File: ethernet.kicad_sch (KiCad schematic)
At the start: 28 parts, among them J1 HR911105A, U4 LAN8742A, Y1 Crystal_GND24

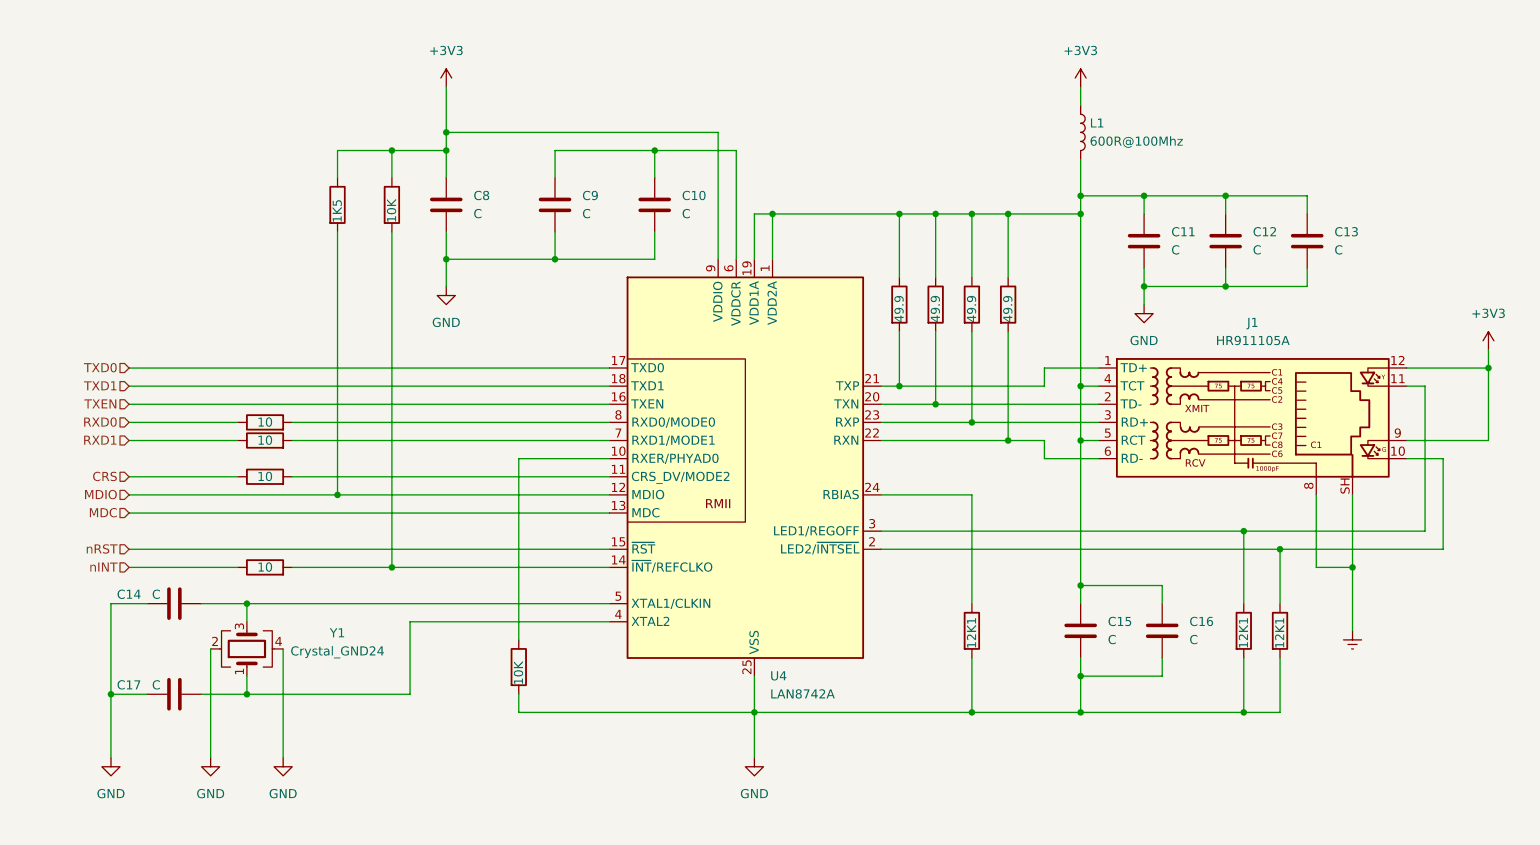
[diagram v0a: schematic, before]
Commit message: Rearranged sheets and corrected some namings
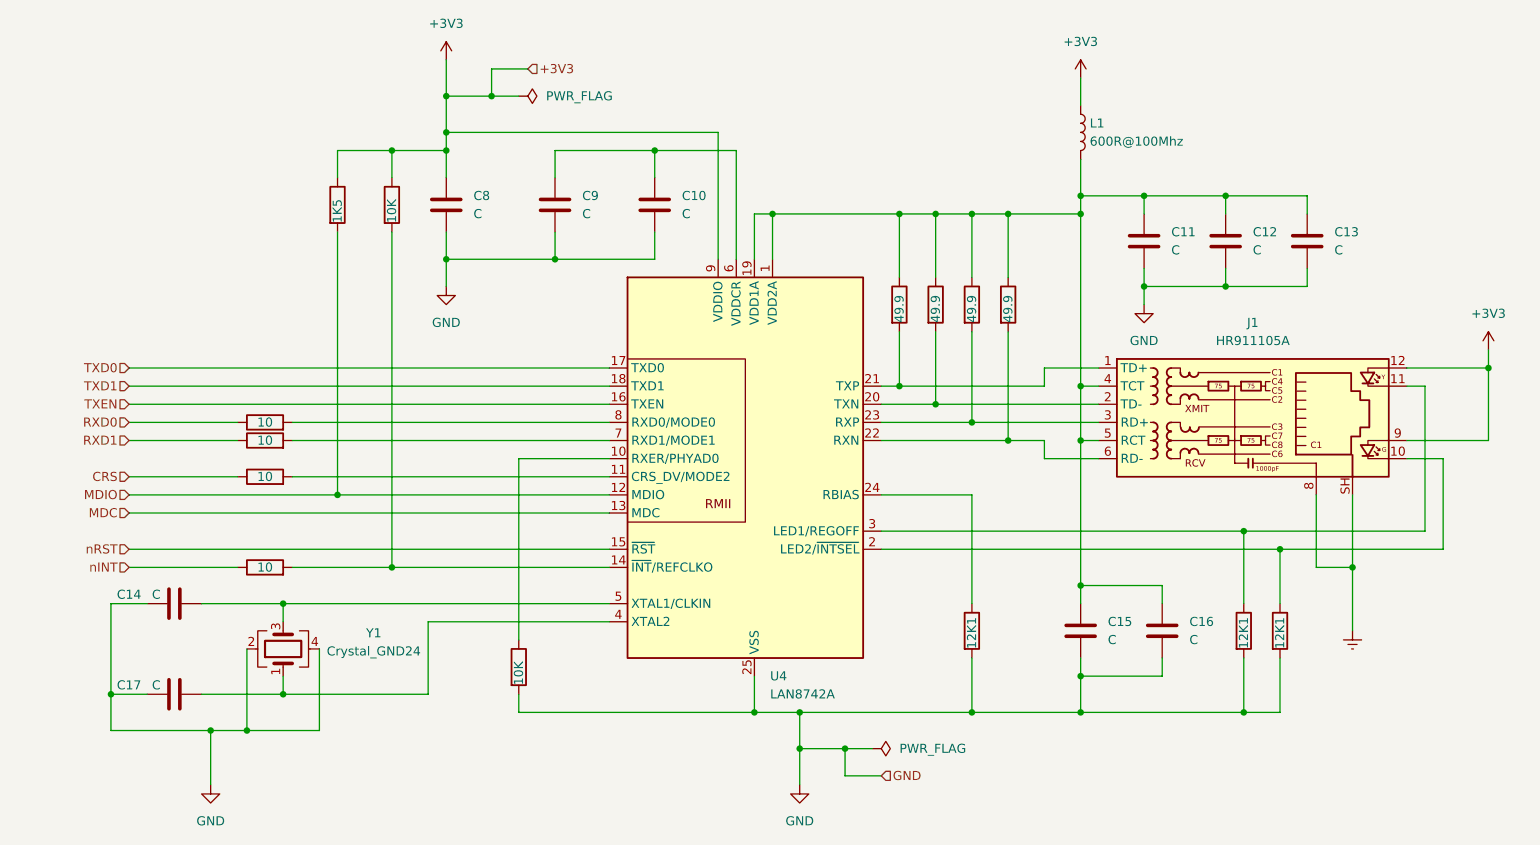
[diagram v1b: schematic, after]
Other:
- moved on the sheet: Y1

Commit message: Finished power setup and cleared some mistakes
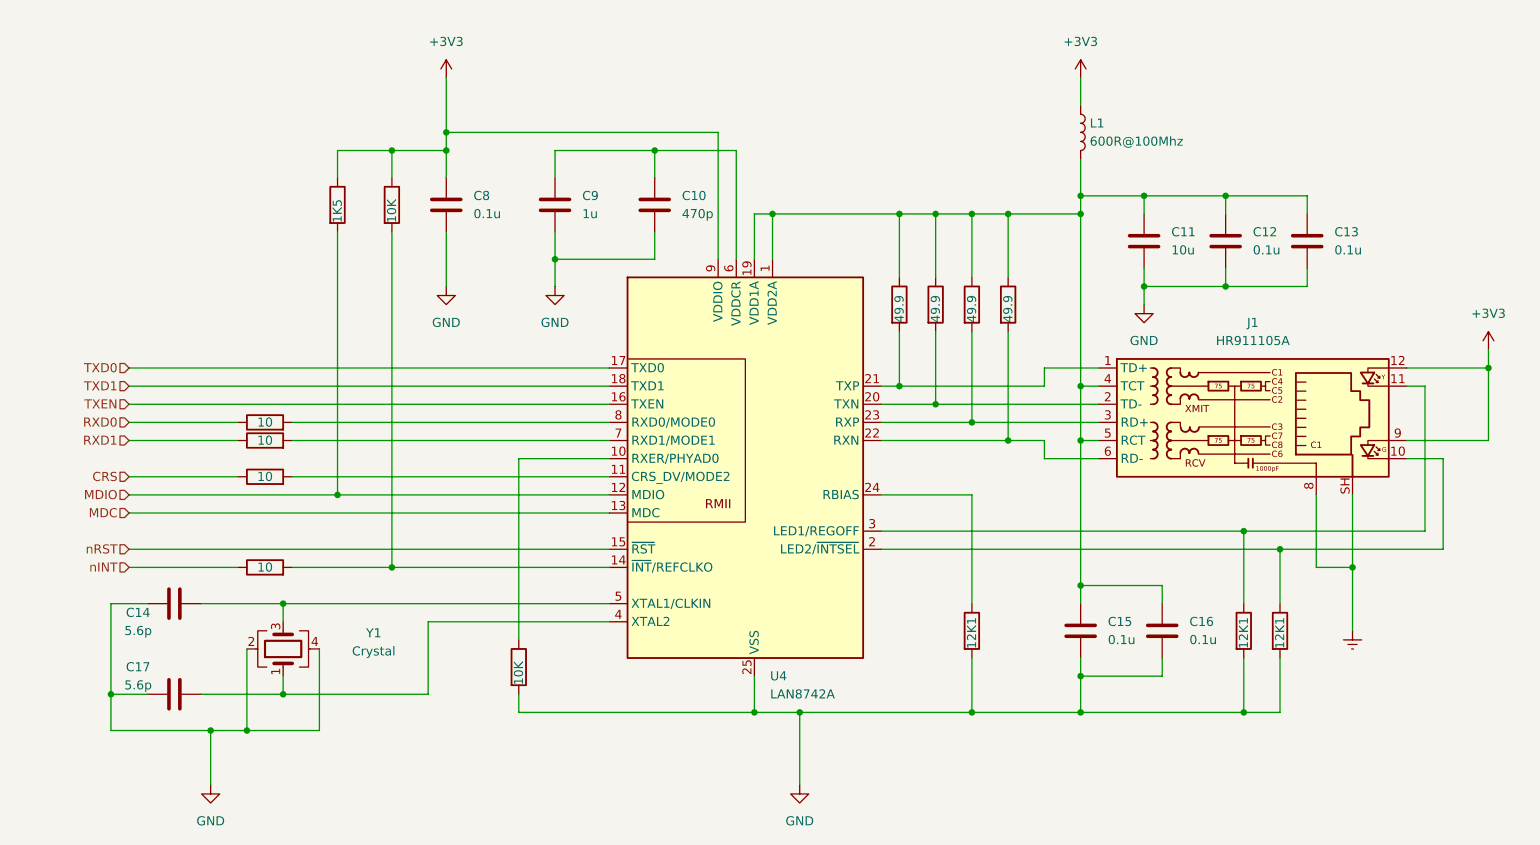
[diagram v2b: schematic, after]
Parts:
- C10: value C -> 470p
- C11: value C -> 10u
- C12, C13, C15, C16, C8: value C -> 0.1u
- C14, C17: value C -> 5.6p
- C9: value C -> 1u
- Y1: value Crystal_GND24 -> Crystal

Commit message: Polished IO schematics
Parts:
- removed R33: 12K1, symbol Device:R
- added R130: 270, symbol Device:R
- R32: value 12K1 -> 270
- Y1: value Crystal -> Crystal 25MHz
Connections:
- net +3V3: no longer J1.12, J1.9
- net GND: now also R130.2
- net at J1.10: now also R32.1; no longer U4.2 (LED2/~{INTSEL})
- net nINT renamed nINT/REFCLK
- new net: J1.9, U4.2 (LED2/~{INTSEL})
- new net: J1.12, U4.3 (LED1/REGOFF)
- new net: J1.11, R130.1
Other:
- moved on the sheet: L1

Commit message: Set power routing for stm32
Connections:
- net +3V3: now also R21.2, R22.2; no longer R21.1, R22.1
- net GND: now also R34.1; no longer R34.2
- net MDIO: now also R21.1; no longer R21.2
- net at R30.2, U4.14 (~{INT}/REFCLKO): now also R22.1; no longer R22.2
- net at U4.10 (RXER/PHYAD0): now also R34.2; no longer R34.1
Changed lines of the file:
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@@
       (effects (font (size 1.27 1.27)) (justify left) hide)
     )
-    (property "Value" "270" (at 251.46 107.95 90)
+    (property "Value" "270" (at 251.5406 107.2876 90)
       (effects (font (size 1.27 1.27)) (justify left))
     )
@@
     )
   )
-  (symbol (lib_id "Device:R") (at 99.06 62.23 0) (unit 1)
-    (in_bom yes) (on_board yes) (dnp no)
-    (property "Reference" "R22" (at 101.6 60.96 0)
-      (effects (font (size 1.27 1.27)) (justify left) hide)
-    )
-    (property "Value" "10K" (at 99.06 64.77 90)
-      (effects (font (size 1.27 1.27)) (justify left))
-    )
-    (property "Footprint" "" (at 97.282 62.23 90)
-      (effects (font (size 1.27 1.27)) hide)
-    )
-    (property "Datasheet" "~" (at 99.06 62.23 0)
-      (effects (font (size 1.27 1.27)) hide)
-    )
-    (pin "2")
-    (pin "1")
-    (instances
-      (project "cad-enc-dec"
-        (path "/894df1c3-1a5d-48b0-9966-84d5c2c2c705/9af4e014-d52c-4337-b318-69a159b803e1"
-          (reference "R22") (unit 1)
-        )
-        (path "/894df1c3-1a5d-48b0-9966-84d5c2c2c705/0c33dc1b-d8bf-494b-9905-02f3a65d6ec6"
-          (reference "R120") (unit 1)
-        )
-      )
-    )
-  )
   (symbol (lib_id "Device:C") (at 227.33 67.31 0) (unit 1)
     (in_bom yes) (on_board yes) (dnp no) (fields_autoplaced)
@@
         (path "/894df1c3-1a5d-48b0-9966-84d5c2c2c705/0c33dc1b-d8bf-494b-9905-02f3a65d6ec6"
           (reference "C34") (unit 1)
+        )
+      )
+    )
+  )
+  (symbol (lib_id "Device:R") (at 116.84 127 180) (unit 1)
+    (in_bom yes) (on_board yes) (dnp no)
+    (property "Reference" "R34" (at 110.49 127 90)
+      (effects (font (size 1.27 1.27)) hide)
+    )
+    (property "Value" "10K" (at 116.84 127 90)
+      (effects (font (size 1.27 1.27)))
+    )
+    (property "Footprint" "" (at 118.618 127 90)
+      (effects (font (size 1.27 1.27)) hide)
+    )
+    (property "Datasheet" "~" (at 116.84 127 0)
+      (effects (font (size 1.27 1.27)) hide)
+    )
+    (pin "2")
+    (pin "1")
+    (instances
+      (project "cad-enc-dec"
+        (path "/894df1c3-1a5d-48b0-9966-84d5c2c2c705/9af4e014-d52c-4337-b318-69a159b803e1"
+          (reference "R34") (unit 1)
+        )
+        (path "/894df1c3-1a5d-48b0-9966-84d5c2c2c705/0c33dc1b-d8bf-494b-9905-02f3a65d6ec6"
+          (reference "R132") (unit 1)
         )
       )
@@
       (effects (font (size 1.27 1.27)) (justify left) hide)
     )
-    (property "Value" "270" (at 256.54 107.95 90)
+    (property "Value" "270" (at 256.5998 107.393 90)
       (effects (font (size 1.27 1.27)) (justify left))
     )
@@
     )
   )
-  (symbol (lib_id "Device:R") (at 116.84 127 0) (unit 1)
-    (in_bom yes) (on_board yes) (dnp no)
-    (property "Reference" "R34" (at 119.38 125.73 0)
-      (effects (font (size 1.27 1.27)) (justify left) hide)
-    )
-    (property "Value" "10K" (at 116.84 129.54 90)
-      (effects (font (size 1.27 1.27)) (justify left))
-    )
-    (property "Footprint" "" (at 115.062 127 90)
-      (effects (font (size 1.27 1.27)) hide)
-    )
-    (property "Datasheet" "~" (at 116.84 127 0)
-      (effects (font (size 1.27 1.27)) hide)
-    )
-    (pin "2")
-    (pin "1")
-    (instances
-      (project "cad-enc-dec"
-        (path "/894df1c3-1a5d-48b0-9966-84d5c2c2c705/9af4e014-d52c-4337-b318-69a159b803e1"
-          (reference "R34") (unit 1)
-        )
-        (path "/894df1c3-1a5d-48b0-9966-84d5c2c2c705/0c33dc1b-d8bf-494b-9905-02f3a65d6ec6"
-          (reference "R132") (unit 1)
+  (symbol (lib_id "Device:R") (at 99.06 62.23 180) (unit 1)
+    (in_bom yes) (on_board yes) (dnp no)
+    (property "Reference" "R22" (at 92.71 62.23 90)
+      (effects (font (size 1.27 1.27)) hide)
+    )
+    (property "Value" "10K" (at 99.06 62.23 90)
+      (effects (font (size 1.27 1.27)))
+    )
+    (property "Footprint" "" (at 100.838 62.23 90)
+      (effects (font (size 1.27 1.27)) hide)
+    )
+    (property "Datasheet" "~" (at 99.06 62.23 0)
+      (effects (font (size 1.27 1.27)) hide)
+    )
+    (pin "2")
+    (pin "1")
+    (instances
+      (project "cad-enc-dec"
+        (path "/894df1c3-1a5d-48b0-9966-84d5c2c2c705/9af4e014-d52c-4337-b318-69a159b803e1"
+          (reference "R22") (unit 1)
+        )
+        (path "/894df1c3-1a5d-48b0-9966-84d5c2c2c705/0c33dc1b-d8bf-494b-9905-02f3a65d6ec6"
+          (reference "R120") (unit 1)
+        )
+      )
+    )
+  )
+  (symbol (lib_id "Device:R") (at 91.44 62.23 180) (unit 1)
+    (in_bom yes) (on_board yes) (dnp no)
+    (property "Reference" "R21" (at 85.09 62.23 90)
+      (effects (font (size 1.27 1.27)) hide)
+    )
+    (property "Value" "1K5" (at 91.44 62.23 90)
+      (effects (font (size 1.27 1.27)))
+    )
+    (property "Footprint" "" (at 93.218 62.23 90)
+      (effects (font (size 1.27 1.27)) hide)
+    )
+    (property "Datasheet" "~" (at 91.44 62.23 0)
+      (effects (font (size 1.27 1.27)) hide)
+    )
+    (pin "2")
+    (pin "1")
+    (instances
+      (project "cad-enc-dec"
+        (path "/894df1c3-1a5d-48b0-9966-84d5c2c2c705/9af4e014-d52c-4337-b318-69a159b803e1"
+          (reference "R21") (unit 1)
+        )
+        (path "/894df1c3-1a5d-48b0-9966-84d5c2c2c705/0c33dc1b-d8bf-494b-9905-02f3a65d6ec6"
+          (reference "R119") (unit 1)
         )
       )
@@
     )
   )
+  (symbol (lib_id "power:Earth") (at 233.68 121.92 0) (unit 1)
+    (in_bom yes) (on_board yes) (dnp no) (fields_autoplaced)
+    (property "Reference" "#PWR073" (at 233.68 128.27 0)
+      (effects (font (size 1.27 1.27)) hide)
+    )
+    (property "Value" "Earth" (at 233.68 125.73 0)
+      (effects (font (size 1.27 1.27)) hide)
+    )
+    (property "Footprint" "" (at 233.68 121.92 0)
+      (effects (font (size 1.27 1.27)) hide)
+    )
+    (property "Datasheet" "~" (at 233.68 121.92 0)
+      (effects (font (size 1.27 1.27)) hide)
+    )
+    (pin "1")
+    (instances
+      (project "cad-enc-dec"
+        (path "/894df1c3-1a5d-48b0-9966-84d5c2c2c705/0c33dc1b-d8bf-494b-9905-02f3a65d6ec6"
+          (reference "#PWR073") (unit 1)
+        )
+        (path "/894df1c3-1a5d-48b0-9966-84d5c2c2c705/9af4e014-d52c-4337-b318-69a159b803e1"
+          (reference "#PWR062") (unit 1)
+        )
+      )
+    )
+  )
   (symbol (lib_id "power:GND") (at 204.47 76.2 0) (unit 1)
     (in_bom yes) (on_board yes) (dnp no) (fields_autoplaced)
@@
         (path "/894df1c3-1a5d-48b0-9966-84d5c2c2c705/0c33dc1b-d8bf-494b-9905-02f3a65d6ec6"
           (reference "R125") (unit 1)
-        )
-      )
-    )
-  )
-  (symbol (lib_id "power:Earth") (at 233.68 121.92 0) (unit 1)
-    (in_bom yes) (on_board yes) (dnp no)
-    (property "Reference" "SHGND" (at 233.68 127 0)
-      (effects (font (size 1.27 1.27)))
-    )
-    (property "Value" "Earth" (at 233.68 125.73 0)
-      (effects (font (size 1.27 1.27)) hide)
-    )
-    (property "Footprint" "" (at 233.68 121.92 0)
-      (effects (font (size 1.27 1.27)) hide)
-    )
-    (property "Datasheet" "~" (at 233.68 121.92 0)
-      (effects (font (size 1.27 1.27)) hide)
-    )
-    (pin "1")
-    (instances
-      (project "cad-enc-dec"
-        (path "/894df1c3-1a5d-48b0-9966-84d5c2c2c705/9af4e014-d52c-4337-b318-69a159b803e1"
-          (reference "SHGND") (unit 1)
-        )
-        (path "/894df1c3-1a5d-48b0-9966-84d5c2c2c705/0c33dc1b-d8bf-494b-9905-02f3a65d6ec6"
-          (reference "#PWR082") (unit 1)
         )
       )
@@
         )
       )
-    )
-  )
-  (symbol (lib_id "Device:R") (at 91.44 62.23 0) (unit 1)
-    (in_bom yes) (on_board yes) (dnp no)
-    (property "Reference" "R21" (at 93.98 60.96 0)
-      (effects (font (size 1.27 1.27)) (justify left) hide)
-    )
-    (property "Value" "1K5" (at 91.44 64.77 90)
-      (effects (font (size 1.27 1.27)) (justify left))
-    )
-    (property "Footprint" "" (at 89.662 62.23 90)
-      (effects (font (size 1.27 1.27)) hide)
-    )
-    (property "Datasheet" "~" (at 91.44 62.23 0)
-      (effects (font (size 1.27 1.27)) hide)
-    )
-    (pin "2")
-    (pin "1")
-    (instances
-      (project "cad-enc-dec"
-        (path "/894df1c3-1a5d-48b0-9966-84d5c2c2c705/9af4e014-d52c-4337-b318-69a159b803e1"
-          (reference "R21") (unit 1)
-        )
-        (path "/894df1c3-1a5d-48b0-9966-84d5c2c2c705/0c33dc1b-d8bf-494b-9905-02f3a65d6ec6"
-          (reference "R119") (unit 1)
-        )
-      )

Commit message: Adjusted components in I/O circuits
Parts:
- added R195, R197, R199, R201: 10K, symbol Device:R
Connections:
- net +3V3: now also R195.2, R197.2, R199.2
- net GND: now also R201.1
- net MDC: now also R195.1
- net at J1.9, U4.2 (LED2/~{INTSEL}): now also R201.2
- net at R28.2, U4.7 (RXD1/MODE1): now also R197.1
- net at R27.2, U4.8 (RXD0/MODE0): now also R199.1
- net nINT/REFCLK renamed REFCLK
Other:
- moved on the sheet: C10, C14, C17

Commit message: Assigned proper footprints for all components
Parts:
- removed Y1: Crystal 25MHz, symbol Device:Crystal_GND24
- added Y3: 25MHz, Crystal:Crystal_SMD_HC49-SD, symbol Device:Crystal
- C10: footprint (none) -> Capacitor_SMD:C_0603_1608Metric_Pad1.08x0.95mm_HandSolder
- C11: footprint (none) -> Capacitor_SMD:C_1206_3216Metric_Pad1.33x1.80mm_HandSolder
- C12, C13, C15, C16, C8: value 0.1u -> 100n; footprint (none) -> Capacitor_SMD:C_0603_1608Metric_Pad1.08x0.95mm_HandSolder
- C14, C17: value 5.6p -> 30p; footprint (none) -> Capacitor_SMD:C_0603_1608Metric_Pad1.08x0.95mm_HandSolder
- C9: footprint (none) -> Capacitor_SMD:C_0805_2012Metric_Pad1.18x1.45mm_HandSolder
- L1: footprint (none) -> Inductor_SMD:L_0603_1608Metric_Pad1.05x0.95mm_HandSolder
- R130, R195, R197, R199, R201, R21, R22, R23, R24, R25, R26, R27, R28, R29, R30, R31, R32, R34: footprint (none) -> Resistor_SMD:R_0603_1608Metric_Pad0.98x0.95mm_HandSolder
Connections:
- net at C14.2, U4.5 (XTAL1/CLKIN): now also Y3.2
- net at C17.2, U4.4 (XTAL2): now also Y3.1
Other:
- moved on the sheet: C14, C17

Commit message: Updated boards hierarchy
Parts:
- renumbered C8 to C17, C9 to C75, C10 to C77, C11 to C79, C12 to C81, C13 to C83, C14 to C87, C15 to C89, C16 to C91, C17 to C93, L1 to L5, R29 to R130, R32 to R185, R130 to R187, R30 to R188, R31 to R189, R201 to R191, R34 to R195, R21 to R23, R199 to R24, R197 to R25, R195 to R26, R22 to R27, R23 to R28, R24 to R29, R25 to R30, R26 to R31, R27 to R32, R28 to R34, U4 to U35, Y3 to Y1

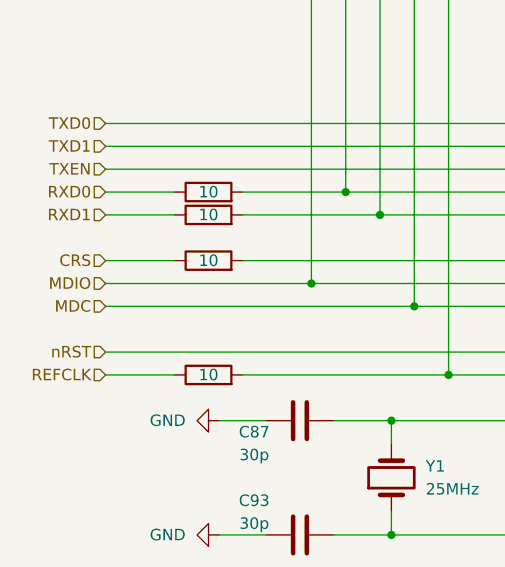
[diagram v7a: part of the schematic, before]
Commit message: Updated ethernet and power IO ports
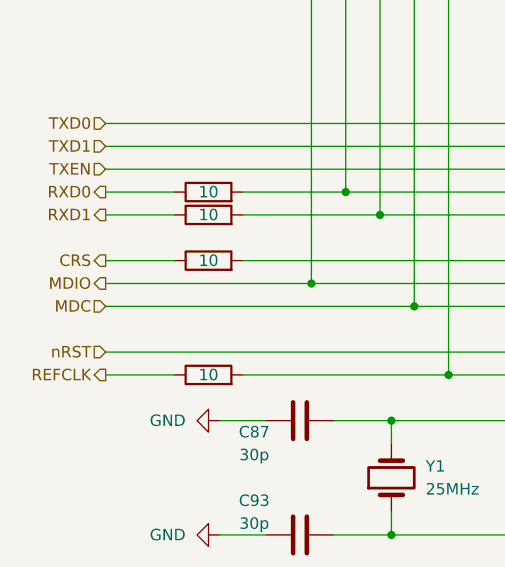
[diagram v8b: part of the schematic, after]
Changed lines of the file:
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@@
     (stroke (width 0) (type default))
   )
-  (hierarchical_label "CRS" (shape input) (at 58.42 100.33 180) (fields_autoplaced)
+  (hierarchical_label "CRS" (shape output) (at 58.42 100.33 180) (fields_autoplaced)
     (effects (font (size 1.27 1.27)) (justify right))
   )
@@
     (effects (font (size 1.27 1.27)) (justify right))
   )
-  (hierarchical_label "REFCLK" (shape input) (at 58.42 113.03 180) (fields_autoplaced)
+  (hierarchical_label "REFCLK" (shape output) (at 58.42 113.03 180) (fields_autoplaced)
     (effects (font (size 1.27 1.27)) (justify right))
   )
-  (hierarchical_label "RXD1" (shape input) (at 58.42 95.25 180) (fields_autoplaced)
+  (hierarchical_label "RXD1" (shape output) (at 58.42 95.25 180) (fields_autoplaced)
     (effects (font (size 1.27 1.27)) (justify right))
   )
-  (hierarchical_label "RXD0" (shape input) (at 58.42 92.71 180) (fields_autoplaced)
+  (hierarchical_label "RXD0" (shape output) (at 58.42 92.71 180) (fields_autoplaced)
     (effects (font (size 1.27 1.27)) (justify right))
   )
@@
     (effects (font (size 1.27 1.27)) (justify right))
   )
-  (hierarchical_label "MDIO" (shape input) (at 58.42 102.87 180) (fields_autoplaced)
+  (hierarchical_label "MDIO" (shape output) (at 58.42 102.87 180) (fields_autoplaced)
     (effects (font (size 1.27 1.27)) (justify right))
   )
